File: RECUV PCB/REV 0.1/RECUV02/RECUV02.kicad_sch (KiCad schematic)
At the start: 14 parts, among them U1 ESP32-S3-WROOM-1, U2 CH340C

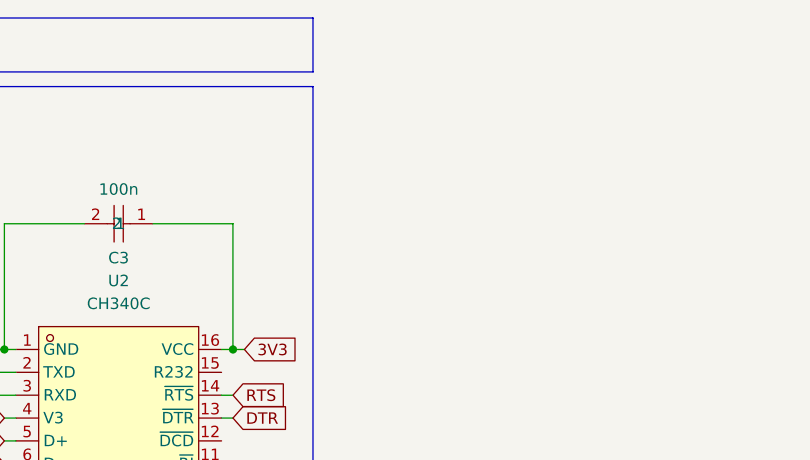
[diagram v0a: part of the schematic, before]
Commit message: Added VEXT Screw Terminal
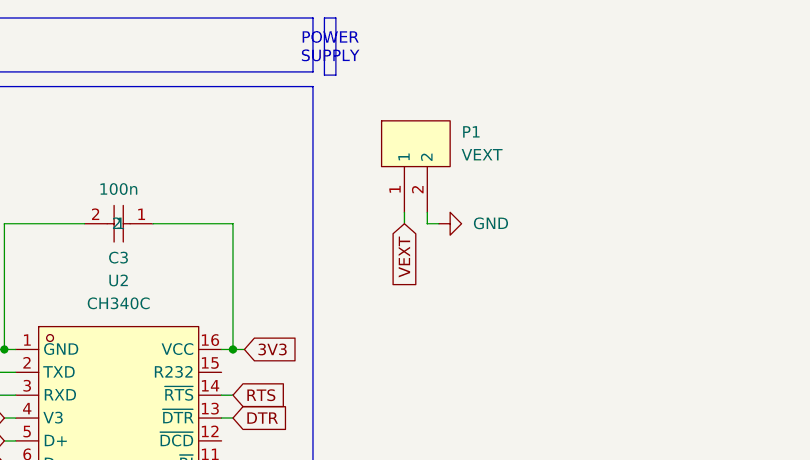
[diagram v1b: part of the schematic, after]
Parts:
- added P1: VEXT, EasyEDA:CONN-TH_2P-P5.00_CPC3703CTR, symbol EasyEDA:WJ127-5.0-2P
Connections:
- net GND: now also P1.2
- new net VEXT: P1.1

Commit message: added Schottky connection
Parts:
- added D1: SS54_C22452, EasyEDA:SMA_L4.4-W2.8-LS5.4-R-RD, symbol EasyEDA:SS54_C22452
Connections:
- net VBUS: now also D1.1 (A)
- net VEXT renamed +5V
- net +5V: now also D1.2 (K)
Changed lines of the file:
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@@
+	)
+	(junction
+		(at 233.68 33.02)
+		(diameter 0)
+		(color 0 0 0 0)
 	)
 	(junction
@@
 	(wire
 		(pts
+			(xy 233.68 33.02) (xy 234.95 33.02)
+		)
+		(stroke
+			(width 0)
+			(type default)
+		)
+	)
+	(wire
+		(pts
 			(xy 68.58 36.83) (xy 69.85 36.83)
 		)
@@
 	(wire
 		(pts
+			(xy 220.98 33.02) (xy 233.68 33.02)
+		)
+		(stroke
+			(width 0)
+			(type default)
+		)
+	)
+	(wire
+		(pts
 			(xy 68.58 44.45) (xy 69.85 44.45)
 		)
@@
 	(wire
 		(pts
+			(xy 233.68 33.02) (xy 233.68 35.56)
+		)
+		(stroke
+			(width 0)
+			(type default)
+		)
+	)
+	(wire
+		(pts
 			(xy 119.38 54.61) (xy 113.03 54.61)
 		)
@@
 	(wire
 		(pts
+			(xy 232.41 35.56) (xy 233.68 35.56)
+		)
+		(stroke
+			(width 0)
+			(type default)
+		)
+	)
+	(wire
+		(pts
 			(xy 113.03 54.61) (xy 113.03 50.8)
 		)
@@
 		)
 	)
+	(wire
+		(pts
+			(xy 220.98 35.56) (xy 222.25 35.56)
+		)
+		(stroke
+			(width 0)
+			(type default)
+		)
+	)
 	(global_label "U0RXD"
 		(shape input)
@@
 		)
 	)
+	(global_label "VEXT"
+		(shape input)
+		(at 220.98 33.02 180)
+		(fields_autoplaced yes)
+		(effects
+			(font
+				(size 1.27 1.27)
+			)
+			(justify right)
+		)
+		(property "Intersheetrefs" "${INTERSHEET_REFS}"
+			(at 213.5801 33.02 0)
+			(hide yes)
+			(show_name no)
+			(do_not_autoplace no)
+			(effects
+				(font
+					(size 1.27 1.27)
+				)
+				(justify right)
+			)
+		)
+	)
 	(global_label "UD+"
 		(shape input)
@@
 		)
 	)
+	(global_label "+5V"
+		(shape input)
+		(at 234.95 33.02 0)
+		(fields_autoplaced yes)
+		(effects
+			(font
+				(size 1.27 1.27)
+			)
+			(justify left)
+		)
+		(property "Intersheetrefs" "${INTERSHEET_REFS}"
+			(at 241.8057 33.02 0)
+			(hide yes)
+			(show_name no)
+			(do_not_autoplace no)
+			(effects
+				(font
+					(size 1.27 1.27)
+				)
+				(justify left)
+			)
+		)
+	)
 	(global_label "UD-"
 		(shape input)
@@
 		(property "Intersheetrefs" "${INTERSHEET_REFS}"
 			(at 96.4377 54.61 0)
+			(hide yes)
+			(show_name no)
+			(do_not_autoplace no)
+			(effects
+				(font
+					(size 1.27 1.27)
+				)
+				(justify right)
+			)
+		)
+	)
+	(global_label "VBUS"
+		(shape input)
+		(at 220.98 35.56 180)
+		(fields_autoplaced yes)
+		(effects
+			(font
+				(size 1.27 1.27)
+			)
+			(justify right)
+		)
+		(property "Intersheetrefs" "${INTERSHEET_REFS}"
+			(at 213.0962 35.56 0)
 			(hide yes)
 			(show_name no)
@@
 					(unit 1)
 				)
+			)
+		)
+	)
+	(symbol
+		(lib_id "EasyEDA:SS54_C22452")
+		(at 227.33 35.56 180)
+		(unit 1)
+		(body_style 1)
+		(exclude_from_sim no)
+		(in_bom yes)
+		(on_board yes)
+		(in_pos_files yes)
+		(dnp no)
+		(fields_autoplaced yes)
+		(property "Reference" "D1"
+			(at 227.71 29.21 0)
+			(show_name no)
+			(do_not_autoplace no)
+			(effects
+				(font
+					(size 1.27 1.27)
+				)
+			)
+		)
+		(property "Value" "SS54_C22452"
+			(at 227.71 31.75 0)
+			(hide yes)
+			(show_name no)
+			(do_not_autoplace no)
+			(effects
+				(font
+					(size 1.27 1.27)
+				)
+			)
+		)
+		(property "Footprint" "EasyEDA:SMA_L4.4-W2.8-LS5.4-R-RD"
+			(at 227.33 27.94 0)
+			(hide yes)
+			(show_name no)
+			(do_not_autoplace no)
+			(effects
+				(font
+					(size 1.27 1.27)
+				)
+			)
+		)
+		(property "Datasheet" "https://lcsc.com/product-detail/Schottky-Barrier-Diodes-SBD_SS54_C22452.html"
+			(at 227.33 25.4 0)
+			(hide yes)
+			(show_name no)
+			(do_not_autoplace no)
+			(effects
+				(font
+					(size 1.27 1.27)
+				)
+			)
+		)
+		(property "Description" "SS54"
+			(at 227.33 35.56 0)
+			(hide yes)
+			(show_name no)
+			(do_not_autoplace no)
+			(effects
+				(font
+					(size 1.27 1.27)
+				)
+			)
+		)
+		(property "Manufacturer" "MDD(辰达半导体)"
+			(at 227.33 22.86 0)
+			(hide yes)
+			(show_name no)
+			(do_not_autoplace no)
+			(effects
+				(font
+					(size 1.27 1.27)
+				)
+			)
+		)
+		(property "MPN" "SS54"
+			(at 227.33 20.32 0)
+			(hide yes)
+			(show_name no)
+			(do_not_autoplace no)
+			(effects
+				(font
+					(size 1.27 1.27)
+				)
+			)
+		)
+		(property "LCSC Part" "C22452"
+			(at 227.33 17.78 0)
+			(hide yes)
+			(show_name no)
+			(do_not_autoplace no)
+			(effects
+				(font
+					(size 1.27 1.27)
+				)
+			)
+		)
+		(pin "2"
+		)
+		(pin "1"
+		)
+		(instances
+			(project "RECUV02"
+				(path "/2b6cdc4d-a2c2-48c0-8972-6d5f3f53de15"
+					(reference "D1")
+					(unit 1)
+				)

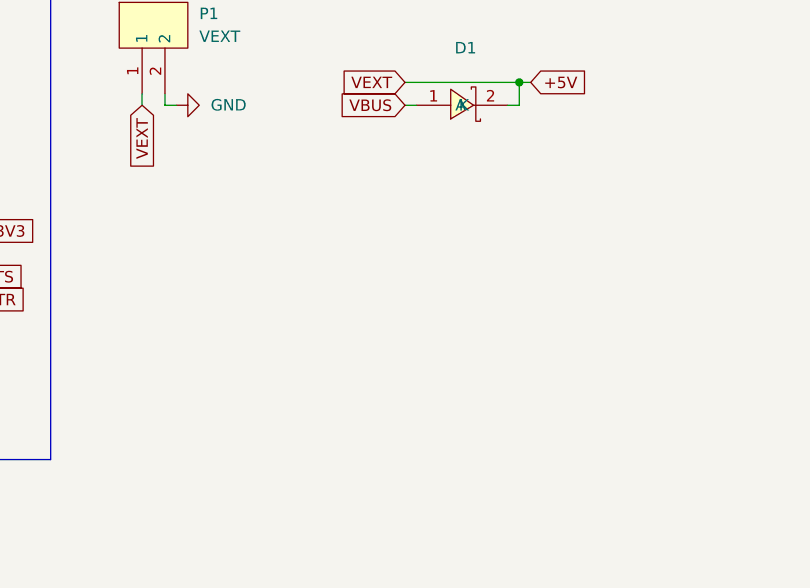
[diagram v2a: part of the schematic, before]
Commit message: Added A1117 and GND
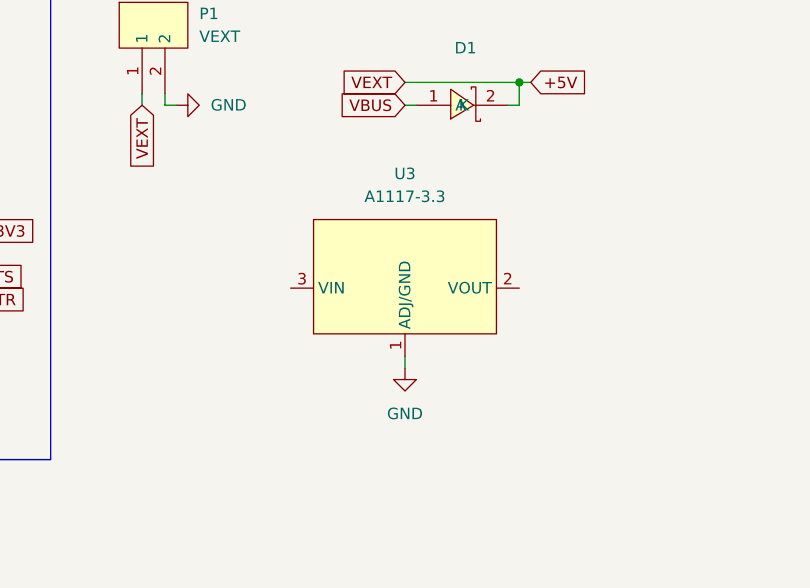
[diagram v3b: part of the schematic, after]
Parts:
- added U3: A1117-3.3, EasyEDA:SOT-223-3_L6.5-W3.4-P2.30-LS7.0-BR-1, symbol EasyEDA:A1117-3.3
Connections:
- net GND: now also U3.1 (ADJ/GND)
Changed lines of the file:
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@@
 	(wire
 		(pts
+			(xy 220.98 63.5) (xy 220.98 64.77)
+		)
+		(stroke
+			(width 0)
+			(type default)
+		)
+	)
+	(wire
+		(pts
 			(xy 39.37 64.77) (xy 40.64 64.77)
 		)
@@
 	)
 	(symbol
+		(lib_id "EasyEDA:A1117-3.3")
+		(at 220.98 55.88 0)
+		(unit 1)
+		(body_style 1)
+		(exclude_from_sim no)
+		(in_bom yes)
+		(on_board yes)
+		(in_pos_files yes)
+		(dnp no)
+		(fields_autoplaced yes)
+		(property "Reference" "U3"
+			(at 220.98 43.18 0)
+			(show_name no)
+			(do_not_autoplace no)
+			(effects
+				(font
+					(size 1.27 1.27)
+				)
+			)
+		)
+		(property "Value" "A1117-3.3"
+			(at 220.98 45.72 0)
+			(show_name no)
+			(do_not_autoplace no)
+			(effects
+				(font
+					(size 1.27 1.27)
+				)
+			)
+		)
+		(property "Footprint" "EasyEDA:SOT-223-3_L6.5-W3.4-P2.30-LS7.0-BR-1"
+			(at 220.98 71.12 0)
+			(hide yes)
+			(show_name no)
+			(do_not_autoplace no)
+			(effects
+				(font
+					(size 1.27 1.27)
+				)
+			)
+		)
+		(property "Datasheet" "https://www.lcsc.com/datasheet/C7432020.pdf"
+			(at 220.98 73.66 0)
+			(hide yes)
+			(show_name no)
+			(do_not_autoplace no)
+			(effects
+				(font
+					(size 1.27 1.27)
+				)
+			)
+		)
+		(property "Description" ""
+			(at 220.98 55.88 0)
+			(hide yes)
+			(show_name no)
+			(do_not_autoplace no)
+			(effects
+				(font
+					(size 1.27 1.27)
+				)
+			)
+		)
+		(property "Manufacturer" "IDCHIP(英锐芯)"
+			(at 220.98 76.2 0)
+			(hide yes)
+			(show_name no)
+			(do_not_autoplace no)
+			(effects
+				(font
+					(size 1.27 1.27)
+				)
+			)
+		)
+		(property "MPN" "A1117-3.3"
+			(at 220.98 78.74 0)
+			(hide yes)
+			(show_name no)
+			(do_not_autoplace no)
+			(effects
+				(font
+					(size 1.27 1.27)
+				)
+			)
+		)
+		(property "LCSC Part" "C7432020"
+			(at 220.98 81.28 0)
+			(hide yes)
+			(show_name no)
+			(do_not_autoplace no)
+			(effects
+				(font
+					(size 1.27 1.27)
+				)
+			)
+		)
+		(pin "3"
+		)
+		(pin "2"
+		)
+		(pin "1"
+		)
+		(instances
+			(project "RECUV02"
+				(path "/2b6cdc4d-a2c2-48c0-8972-6d5f3f53de15"
+					(reference "U3")
+					(unit 1)
+				)
+			)
+		)
+	)
+	(symbol
 		(lib_id "EasyEDA:0805W8J0512T5E")
 		(at 27.94 46.99 180)
@@
 					(unit 1)
 				)
+			)
+		)
+	)
+	(symbol
+		(lib_id "power:GND")
+		(at 220.98 64.77 0)
+		(unit 1)
+		(body_style 1)
+		(exclude_from_sim no)
+		(in_bom yes)
+		(on_board yes)
+		(in_pos_files yes)
+		(dnp no)
+		(fields_autoplaced yes)
+		(property "Reference" "#PWR012"
+			(at 220.98 71.12 0)
+			(hide yes)
+			(show_name no)
+			(do_not_autoplace no)
+			(effects
+				(font
+					(size 1.27 1.27)
+				)
+			)
+		)
+		(property "Value" "GND"
+			(at 220.98 69.85 0)
+			(show_name no)
+			(do_not_autoplace no)
+			(effects
+				(font
+					(size 1.27 1.27)
+				)
+			)
+		)
+		(property "Footprint" ""
+			(at 220.98 64.77 0)
+			(hide yes)
+			(show_name no)
+			(do_not_autoplace no)
+			(effects
+				(font
+					(size 1.27 1.27)
+				)
+			)
+		)
+		(property "Datasheet" ""
+			(at 220.98 64.77 0)
+			(hide yes)
+			(show_name no)
+			(do_not_autoplace no)
+			(effects
+				(font
+					(size 1.27 1.27)
+				)
+			)
+		)
+		(property "Description" "Power symbol creates a global label with name \"GND\" , ground"
+			(at 220.98 64.77 0)
+			(hide yes)
+			(show_name no)
+			(do_not_autoplace no)
+			(effects
+				(font
+					(size 1.27 1.27)
+				)
+			)
+		)
+		(pin "1"
+		)
+		(instances
+			(project "RECUV02"
+				(path "/2b6cdc4d-a2c2-48c0-8972-6d5f3f53de15"
+					(reference "#PWR012")
+					(unit 1)
+				)

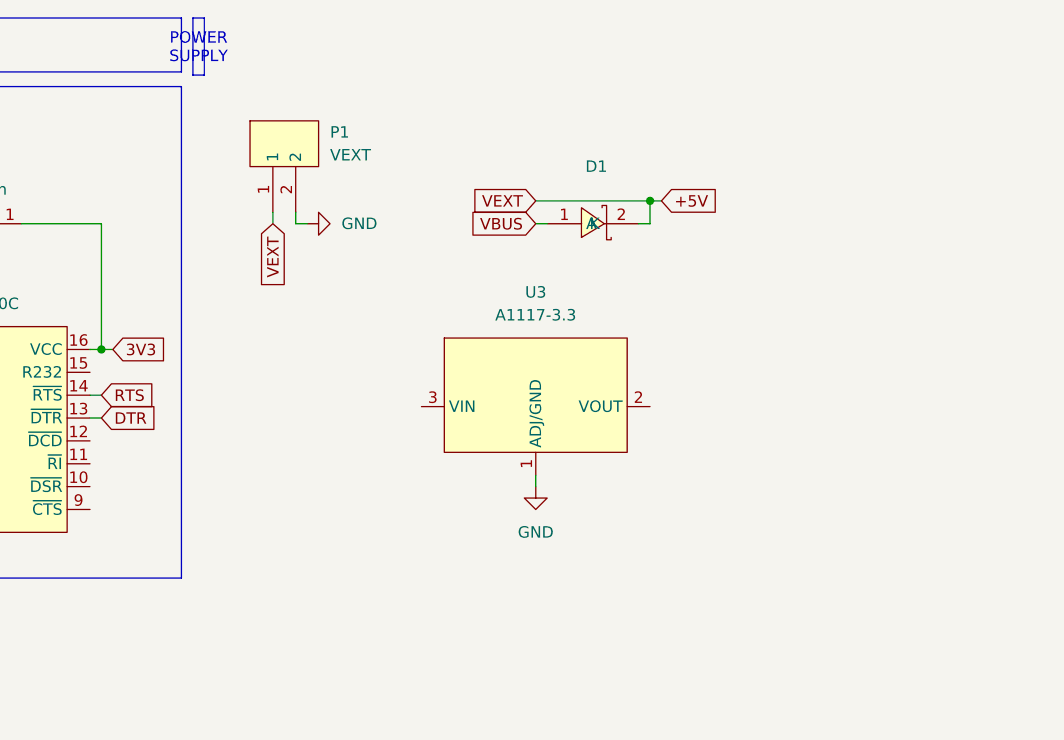
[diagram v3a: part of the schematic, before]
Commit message: Finished Power Supply Section
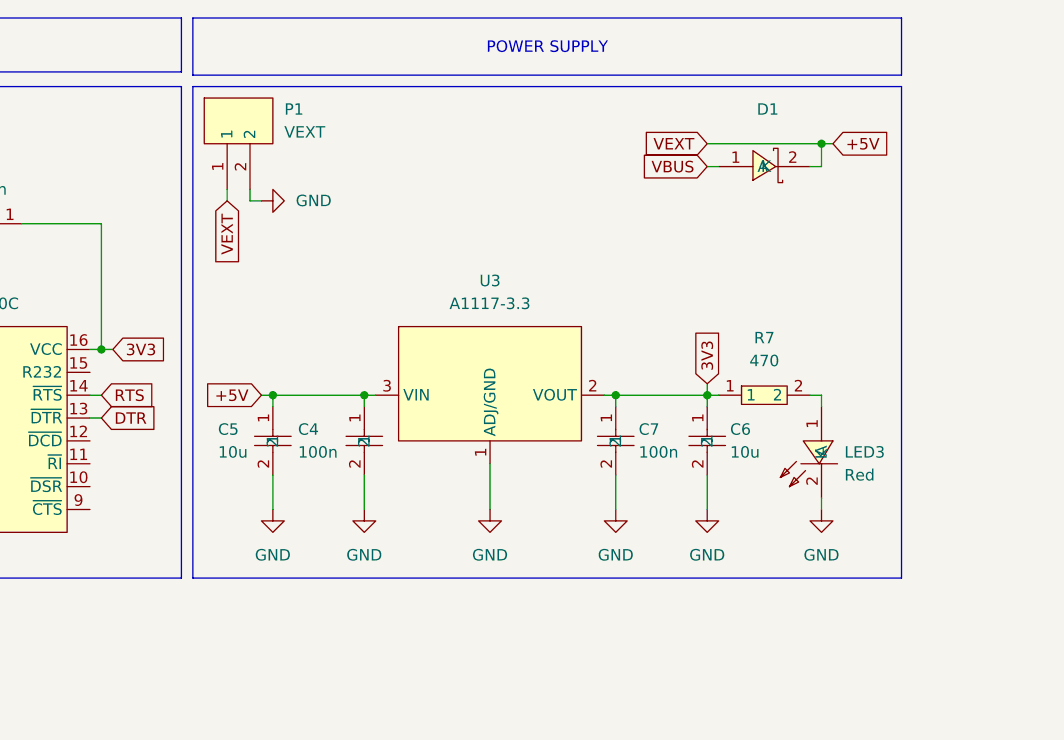
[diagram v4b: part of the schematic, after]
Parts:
- added C4, C7: 100n, EasyEDA:C0805, symbol EasyEDA:CL21B104KBCNNNC
- added C5, C6: 10u, EasyEDA:C0805, symbol EasyEDA:CL21A106KOQNNNE
- added LED3: Red, EasyEDA:LED0805-R-RD, symbol EasyEDA:E6C0805UR
- added R7: 470, EasyEDA:R0805, symbol EasyEDA:0805W8F4700T5E
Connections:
- net +5V: now also U3.3 (VIN), C4.1, C5.1
- net 3V3: now also U3.2 (VOUT), C6.1, C7.1, R7.1
- net GND: now also C4.2, C5.2, C6.2, C7.2, LED3.2 (K)
- new net: LED3.1 (A), R7.2
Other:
- moved on the sheet: D1, P1, U3

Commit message: Finished Boot Settings
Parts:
- added C8, C9: 100n, EasyEDA:C0805, symbol EasyEDA:CL21B104KBCNNNC
- added Q1, Q2: MMBT2222ALT1, EasyEDA:SOT-23-3_L3.0-W1.7-P0.95-LS2.9-BR, symbol EasyEDA:MMBT2222ALT1
- added R8, R9: 10k, EasyEDA:R0805, symbol EasyEDA:0805W8F1002T5E
- added U4: RESET, EasyEDA:SW-SMD_KSR213GLFG, symbol EasyEDA:KSR213GLFG
- added U5: BOOT, EasyEDA:SW-SMD_KSR213GLFG, symbol EasyEDA:KSR213GLFG
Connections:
- net DTR: now also Q2.2 (E), R8.1
- net GND: now also C8.2, C9.2, U4.1, U5.1
- net RTS: now also Q1.2 (E), R9.1
- new net: Q1.1 (B), R8.2
- new net: Q2.1 (B), R9.2
- new net CHIP_PU: C8.1, Q1.3 (C), U4.2
- new net GPIO00: C9.1, Q2.3 (C), U5.2

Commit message: Added ESP32S3 left row pins
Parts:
- added C10: 10u, EasyEDA:C0805, symbol EasyEDA:CL21A106KOQNNNE
- added C11: 100n, EasyEDA:C0805, symbol EasyEDA:CL21B104KBCNNNC
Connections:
- net 3V3: now also U1.2 (3V3), C10.1, C11.1
- net CHIP_PU: now also U1.3 (EN)
- net GND: now also U1.1 (GND), C10.2, C11.2
- net GPIO17: now reaches U1.10 (IO17)
- net GPIO18: now reaches U1.11 (IO18)
- net GPIO08: now reaches U1.12 (IO8)
- net GPIO19: now reaches U1.13 (IO19)
- net GPIO20: now reaches U1.14 (IO20)
- net GPIO04: now reaches U1.4 (IO4)
- net GPIO05: now reaches U1.5 (IO5)
- net GPIO06: now reaches U1.6 (IO6)
- net GPIO07: now reaches U1.7 (IO7)
- net GPIO15: now reaches U1.8 (IO15)
- net GPIO16: now reaches U1.9 (IO16)
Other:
- moved on the sheet: U1

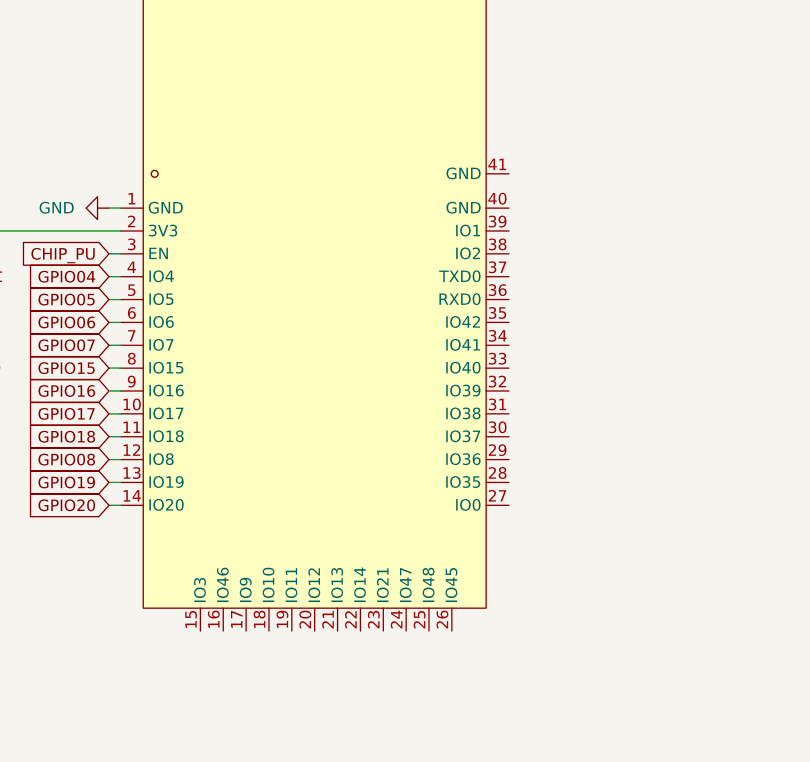
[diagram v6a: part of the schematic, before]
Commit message: Added all PINs to ESP32S3
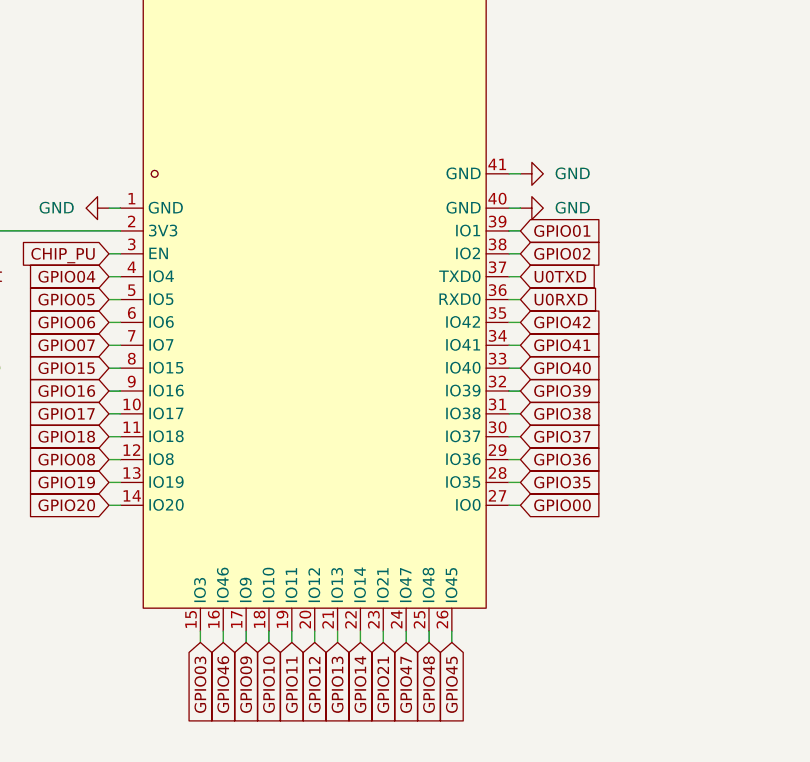
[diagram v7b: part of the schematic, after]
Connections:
- net GND: now also U1.40 (GND), U1.41 (GND)
- net GPIO00: now also U1.27 (IO0)
- net U0RXD: now also U1.36 (RXD0)
- net U0TXD: now also U1.37 (TXD0)
- net GPIO03: now reaches U1.15 (IO3)
- net GPIO46: now reaches U1.16 (IO46)
- net GPIO09: now reaches U1.17 (IO9)
- net GPIO10: now reaches U1.18 (IO10)
- net GPIO11: now reaches U1.19 (IO11)
- net GPIO12: now reaches U1.20 (IO12)
- net GPIO13: now reaches U1.21 (IO13)
- net GPIO14: now reaches U1.22 (IO14)
- net GPIO21: now reaches U1.23 (IO21)
- net GPIO47: now reaches U1.24 (IO47)
- net GPIO48: now reaches U1.25 (IO48)
- net GPIO45: now reaches U1.26 (IO45)
- net GPIO35: now reaches U1.28 (IO35)
- net GPIO36: now reaches U1.29 (IO36)
- net GPIO37: now reaches U1.30 (IO37)
- net GPIO38: now reaches U1.31 (IO38)
- net GPIO39: now reaches U1.32 (IO39)
- net GPIO40: now reaches U1.33 (IO40)
- net GPIO41: now reaches U1.34 (IO41)
- net GPIO42: now reaches U1.35 (IO42)
- net GPIO02: now reaches U1.38 (IO2)
- net GPIO01: now reaches U1.39 (IO1)

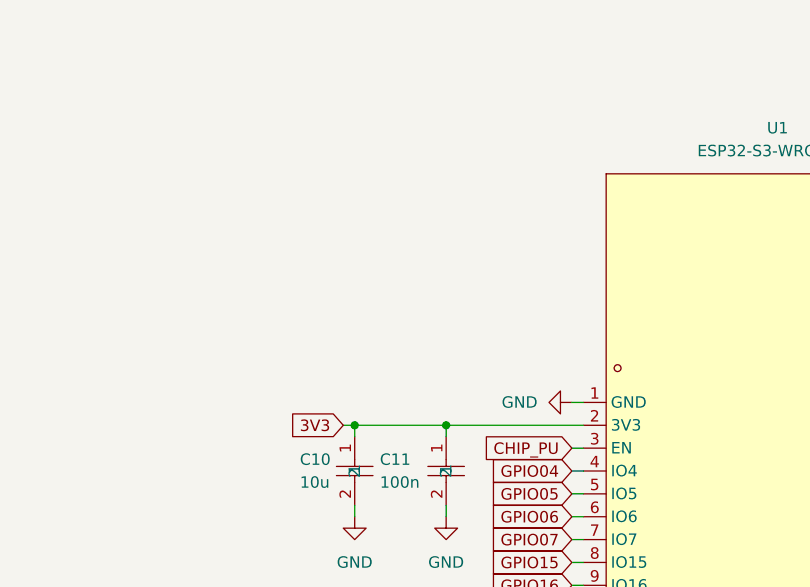
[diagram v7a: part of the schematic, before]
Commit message: Added CHIP_PU capacitor
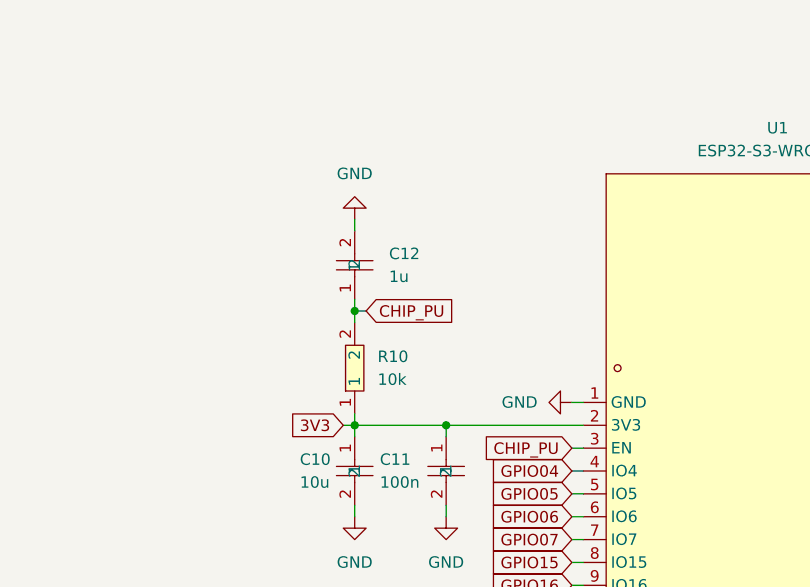
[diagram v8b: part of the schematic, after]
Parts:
- added C12: 1u, EasyEDA:C0805, symbol EasyEDA:CL21B105KAFNFNE
- added R10: 10k, EasyEDA:R0805, symbol EasyEDA:0805W8F1002T5E
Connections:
- net 3V3: now also R10.1
- net CHIP_PU: now also C12.1, R10.2
- net GND: now also C12.2
